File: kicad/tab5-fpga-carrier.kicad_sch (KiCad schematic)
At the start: 77 parts, among them J1 DC 12-24V, J2 USB-C PD in, J3 M5-BUS (to Tab5), J4 Tang Primer 20K Core, J5 HDMI OUT, J6 PMOD1, J7 PMOD2, J8 FPGA JTAG, Q1 2N7002, Q2 2N7002, SW1 SW, SW2 SW, U1 CH224K, U2 TPS5430DDAR, U3 AMS1117-3.3

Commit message: kicad: layout v1.0 (Core left of M5-Bus, HDMI bottom edge, pin swap), 106/106 routed, DRC clean; reset/power switch/GPIO pads; docs
Co-Authored-By: Claude Sonnet 5.5 <noreply@anthropic.com>
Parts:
- removed C7: 47u/10V, Capacitor_SMD:C_1206_3216Metric, symbol Device:C
- removed J8: FPGA JTAG, Connector_PinHeader_2.54mm:PinHeader_1x06_P2.54mm_Vertical, symbol Connector_Generic:Conn_01x06
- added C11: 22u/10V, Capacitor_SMD:C_1206_3216Metric, symbol Device:C
- added C7: 220u/10V polymer, Capacitor_SMD:CP_Elec_6.3x7.7, symbol Device:C_Polarized
- added H5, H6: M3, MountingHole:MountingHole_3.2mm_M3, symbol Mechanical:MountingHole
- added J8: GPIO pads, Connector_PinHeader_2.54mm:PinHeader_1x09_P2.54mm_Vertical, symbol Connector_Generic:Conn_01x09
- added SW3: RESET (Tab5), Button_Switch_SMD:SW_SPST_EVQP0, symbol Switch:SW_Push
- added SW4: FPGA ON/OFF, Button_Switch_THT:SW_DIP_SPSTx01_Slide_9.78x4.72mm_W7.62mm_P2.54mm, symbol Switch:SW_DIP_x01
- C10: value 22u/10V -> 10u/16V
- C9: value 10u/16V -> 47u/10V
- J6, J7: Comment 2x6 PMOD-style, 3.3V -> 2x6 PMOD-style, 3.3V. Pads only: pin header is hand-fitted 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; now not fitted
- R16: value 33R -> 0R; Comment (none) -> 16-bit extension (DNP): connects G37 to FPGA; now not fitted
- R17: value 33R -> 0R; Comment (none) -> 16-bit extension (DNP): connects G38 to FPGA; now not fitted
- R26: value 0R -> 33R; Comment 16-bit extension (DNP): connects G37 to FPGA -> (none); now fitted
- R27: value 0R -> 33R; Comment 16-bit extension (DNP): connects G38 to FPGA -> (none); now fitted
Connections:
- net +3V3: now also C11.1, J8.1 (Pin_1); no longer C10.1
- net +5V: now also C10.1, C7.1
- net BUCK_EN: now also SW4.1
- net F_AUX0: now also J4.119 (F_AUX0), R10.2; no longer J4.101 (F_AUX0), R21.2
- net F_AUX1: now also J4.109 (F_AUX1), R13.2; no longer J4.103 (F_AUX1), R22.2
- net F_AUX2: now also J4.95 (F_AUX2), R18.2; no longer J4.107 (F_AUX2), R23.2
- net F_AUX3: now also J4.91 (F_AUX3), R19.2; no longer J4.109 (F_AUX3), R24.2
- net F_BTN1: now also J4.28 (F_BTN1); no longer J4.76 (F_BTN1)
- net F_CLK: now also R23.2; no longer R14.2
- net F_D0: now also J4.113 (F_D0), R12.2; no longer J4.73 (F_D0), R10.2
- net F_D1: now also J4.107 (F_D1), R14.2; no longer J4.75 (F_D1), R11.2
- net F_D2: now also J4.103 (F_D2), R15.2; no longer J4.77 (F_D2), R12.2
- net F_D3: now also J4.85 (F_D3), R21.2; no longer J4.79 (F_D3), R13.2
- net F_D4: now also J4.89 (F_D4), R20.2; no longer J4.83 (F_D4), R15.2
- net F_D5: now also J4.79 (F_D5), R24.2; no longer J4.85 (F_D5), R16.2
- net F_D6: now also J4.83 (F_D6), R22.2; no longer J4.89 (F_D6), R17.2
- net F_D7: now also J4.75 (F_D7), R26.2; no longer J4.91 (F_D7), R18.2
- net F_DIR: now also J4.73 (F_DIR), R27.2; no longer J4.97 (F_DIR), R20.2
- net F_EXT35: now also J4.77 (F_EXT35); no longer J4.113 (F_EXT35)
- net F_EXT37: now also J4.101 (F_EXT37), R16.2; no longer J4.115 (F_EXT37), R26.2
- net F_EXT38: now also J4.97 (F_EXT38), R17.2; no longer J4.119 (F_EXT38), R27.2
- net F_HPD: now also J4.30 (F_HPD); no longer J4.78 (F_HPD)
- net F_HSCL: now also J4.36 (F_HSCL); no longer J4.152 (F_HSCL)
- net F_HSDA: now also J4.34 (F_HSDA); no longer J4.154 (F_HSDA)
- net F_LED0: now also J4.146 (F_LED0); no longer J4.50 (F_LED0)
- net F_LED1: now also J4.148 (F_LED1); no longer J4.52 (F_LED1)
- net F_LED2: now also J4.152 (F_LED2); no longer J4.56 (F_LED2)
- net F_LED3: now also J4.154 (F_LED3); no longer J4.58 (F_LED3)
- net F_RDY: now also J4.115 (F_RDY), R11.2; no longer J4.95 (F_RDY), R19.2
- net GND: now also C11.2, C7.2, J8.2 (Pin_2), SW3.2, SW4.2
- net HDMI_CKN: now also J4.142 (HDMI_CKN); no longer J4.62 (HDMI_CKN)
- net HDMI_CKP: now also J4.140 (HDMI_CKP); no longer J4.64 (HDMI_CKP)
- net HDMI_D0N: now also J4.62 (HDMI_D0N); no longer J4.142 (HDMI_D0N)
- net HDMI_D0P: now also J4.64 (HDMI_D0P); no longer J4.140 (HDMI_D0P)
- net HDMI_D1N: now also J4.70 (HDMI_D1N); no longer J4.132 (HDMI_D1N)
- net HDMI_D1P: now also J4.68 (HDMI_D1P); no longer J4.130 (HDMI_D1P)
- net HDMI_D2N: now also J4.132 (HDMI_D2N); no longer J4.70 (HDMI_D2N)
- net HDMI_D2P: now also J4.130 (HDMI_D2P); no longer J4.68 (HDMI_D2P)
- net M_AUX0: now also R10.1; no longer R21.1
- net M_AUX1: now also R13.1; no longer R22.1
- net M_AUX2: now also R18.1; no longer R23.1
- net M_AUX3: now also R19.1; no longer R24.1
- net M_CLK: now also R23.1; no longer R14.1
- net M_D0: now also R12.1; no longer R10.1
- net M_D1: now also R14.1; no longer R11.1
- net M_D2: now also R15.1; no longer R12.1
- net M_D3: now also R21.1; no longer R13.1
- net M_D4: now also R20.1; no longer R15.1
- net M_D5: now also R24.1; no longer R16.1
- net M_D6: now also R22.1; no longer R17.1
- net M_D7: now also R26.1; no longer R18.1
- net M_DIR: now also R27.1; no longer R20.1
- net M_EXT37: now also R16.1; no longer R26.1
- net M_EXT38: now also R17.1; no longer R27.1
- net M_RDY: now also R11.1; no longer R19.1
- net P1_0: now also J4.123 (P1_0); no longer J4.121 (P1_0)
- net P1_1: now also J4.92 (P1_1); no longer J4.123 (P1_1)
- net P1_2: now also J4.86 (P1_2); no longer J4.125 (P1_2)
- net P1_3: now also J4.78 (P1_3); no longer J4.129 (P1_3)
- net P1_4: now also J4.121 (P1_4); no longer J4.131 (P1_4)
- net P1_5: now also J4.90 (P1_5); no longer J4.84 (P1_5)
- net P1_6: now also J4.84 (P1_6); no longer J4.44 (P1_6)
- net P1_7: now also J4.76 (P1_7); no longer J4.46 (P1_7)
- net P2_0: now also J4.58 (P2_0); no longer J4.28 (P2_0)
- net P2_1: now also J4.52 (P2_1); no longer J4.30 (P2_1)
- net P2_2: now also J4.46 (P2_2); no longer J4.34 (P2_2)
- net P2_3: now also J4.42 (P2_3); no longer J4.36 (P2_3)
- net P2_4: now also J4.56 (P2_4); no longer J4.40 (P2_4)
- net P2_5: now also J4.50 (P2_5); no longer J4.42 (P2_5)
- net P2_6: now also J4.44 (P2_6); no longer J4.148 (P2_6)
- net P2_7: now also J4.40 (P2_7); no longer J4.146 (P2_7)
- net TAB_RST: now also SW3.1
- net GPIO3: now reaches J4.176 (GPIO3)
- net GPIO3: now also J8.6 (Pin_6)
- net GPIO2: now reaches J4.180 (GPIO2)
- net GPIO2: now also J8.5 (Pin_5)
- net GPIO1: now reaches J4.182 (GPIO1)
- net GPIO1: now also J8.4 (Pin_4)
- net GPIO0: now reaches J4.186 (GPIO0)
- net GPIO0: now also J8.3 (Pin_3)
- net JT_TCK: no longer names the net of J4.149
- net JT_TDI: no longer names the net of J4.153
- net JT_TDO: no longer names the net of J4.147
- net JT_TMS: no longer names the net of J4.143
- new net GPIO4: J4.131 (GPIO4), J8.7 (Pin_7)
- new net GPIO5: J4.129 (GPIO5), J8.8 (Pin_8)
- new net GPIO6: J4.125 (GPIO6), J8.9 (Pin_9)
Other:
- note added: "Spare FPGA I/O pads"

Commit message: kicad v2.0: Core right of M-Bus, HDMI right edge, official-Dock HDMI circuit (AC coupling/499R/ESD), coupled TMDS pair routing, 121/121 routed, DRC clean; HDMI SI study + docs/site
Co-Authored-By: Claude Sonnet 5.5 <noreply@anthropic.com>
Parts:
- removed SW3: RESET (Tab5), Button_Switch_SMD:SW_SPST_EVQP0, symbol Switch:SW_Push
- removed SW4: FPGA ON/OFF, Button_Switch_THT:SW_DIP_SPSTx01_Slide_9.78x4.72mm_W7.62mm_P2.54mm, symbol Switch:SW_DIP_x01
- added C12, C13, C14, C15, C16, C17, C18, C19: 100n, Capacitor_SMD:C_0603_1608Metric, symbol Device:C
- added R38, R39: 2.2k, Resistor_SMD:R_0603_1608Metric, symbol Device:R
- added R40: 10k, Resistor_SMD:R_0603_1608Metric, symbol Device:R
- added R41: 20k, Resistor_SMD:R_0603_1608Metric, symbol Device:R
- added R42, R43, R44, R45: 1k, Resistor_SMD:R_0603_1608Metric, symbol Device:R
- added SW3: FPGA ON/OFF, Button_Switch_THT:SW_DIP_SPSTx01_Slide_9.78x4.72mm_W7.62mm_P2.54mm, symbol Switch:SW_DIP_x01
- added U4, U5: RCLAMP0524P, Package_SON:USON-10_2.5x1.0mm_P0.5mm, symbol carrier:RCLAMP0524P
- added U6: SRV05-4, Package_TO_SOT_SMD:SOT-23-6, symbol Power_Protection:SRV05-4
- J5: Comment TMDS driven directly by FPGA true-LVDS outputs (3.3V bank) -> TMDS from FPGA true-LVDS outputs (3.3V bank), AC coupled + 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
- R16: value 0R -> 33R; Comment 16-bit extension (DNP): connects G37 to FPGA -> (none); now fitted
- R17: Comment 16-bit extension (DNP): connects G38 to FPGA -> 16-bit extension (DNP): connects G37 to FPGA
- R18: value 33R -> 0R; Comment (none) -> 16-bit extension (DNP): connects G38 to FPGA; now not fitted
- R28, R29, R32: value 10k -> 499R
- R30, R31: value 2.2k -> 499R
- R33: value 20k -> 499R
- R34, R35: value 1k -> 499R
- R36, R37: value 1k -> 10k
- SW2: value SW -> RESET (Tab5); Comment (none) -> pulls the M5-Bus RST/EN line (pin 6) low: resets the ESP32-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
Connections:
- net +3V3: now also R36.1, R37.1; no longer R28.1, R29.1
- net BUCK_EN: now also SW3.1
- net F_AUX0: now also J4.73 (F_AUX0); no longer J4.119 (F_AUX0)
- net F_AUX1: now also J4.79 (F_AUX1); no longer J4.109 (F_AUX1)
- net F_AUX2: now also R19.2; no longer R18.2
- net F_AUX3: now also J4.97 (F_AUX3), R20.2; no longer J4.91 (F_AUX3), R19.2
- net F_CLK: now also R14.2; no longer R23.2
- net F_D0: now also J4.77 (F_D0); no longer J4.113 (F_D0)
- net F_D1: now also J4.83 (F_D1), R15.2; no longer J4.107 (F_D1), R14.2
- net F_D2: now also J4.85 (F_D2), R16.2; no longer J4.103 (F_D2), R15.2
- net F_D3: now also J4.103 (F_D3), R22.2; no longer J4.85 (F_D3), R21.2
- net F_D4: now also J4.101 (F_D4), R21.2; no longer J4.89 (F_D4), R20.2
- net F_D5: now also J4.109 (F_D5); no longer J4.79 (F_D5)
- net F_D6: now also J4.107 (F_D6), R23.2; no longer J4.83 (F_D6), R22.2
- net F_D7: now also J4.115 (F_D7); no longer J4.75 (F_D7)
- net F_DIR: now also J4.119 (F_DIR); no longer J4.73 (F_DIR)
- net F_EXT35: now also J4.113 (F_EXT35); no longer J4.77 (F_EXT35)
- net F_EXT37: now also J4.89 (F_EXT37), R17.2; no longer J4.101 (F_EXT37), R16.2
- net F_EXT38: now also J4.91 (F_EXT38), R18.2; no longer J4.97 (F_EXT38), R17.2
- net F_HPD: now also R40.2, R41.1; no longer R32.2, R33.1
- net F_HSCL: now also R36.2; no longer R28.2
- net F_HSDA: now also R37.2; no longer R29.2
- net F_LED0: now also R42.1; no longer R34.1
- net F_LED1: now also R43.1; no longer R35.1
- net F_LED2: now also R44.1; no longer R36.1
- net F_LED3: now also R45.1; no longer R37.1
- net F_RDY: now also J4.75 (F_RDY); no longer J4.115 (F_RDY)
- net GND: now also R28.2, R29.2, R30.2, R31.2, R32.2, R34.2, R35.2, R41.2, SW3.2, U4.3 (GND), U4.8 (GND), U5.3 (GND), U5.8 (GND), U6.2 (VN)
- net GPIO0: now also J4.125 (GPIO0); no longer J4.186 (GPIO0)
- net GPIO1: now also J4.129 (GPIO1); no longer J4.182 (GPIO1)
- net GPIO2: now also J4.131 (GPIO2); no longer J4.180 (GPIO2)
- net GPIO4: now also J4.180 (GPIO4); no longer J4.131 (GPIO4)
- net GPIO5: now also J4.182 (GPIO5); no longer J4.129 (GPIO5)
- net GPIO6: now also J4.186 (GPIO6); no longer J4.125 (GPIO6)
- net HDMI_5V: now also R38.1, R39.1, U6.5 (VP); no longer R30.1, R31.1
- net HDMI_CKN: now also C19.1; no longer J5.12 (CK-)
- net HDMI_CKP: now also C18.1; no longer J5.10 (CK+)
- net HDMI_D0N: now also J4.132 (HDMI_D0N), C17.1; no longer J4.62 (HDMI_D0N), J5.9 (D0-)
- net HDMI_D0P: now also J4.130 (HDMI_D0P), C16.1; no longer J4.64 (HDMI_D0P), J5.7 (D0+)
- net HDMI_D1N: now also C15.1; no longer J5.6 (D1-)
- net HDMI_D1P: now also C14.1; no longer J5.4 (D1+)
- net HDMI_D2N: now also J4.58 (HDMI_D2N), C13.1; no longer J4.132 (HDMI_D2N), J5.3 (D2-)
- net HDMI_D2P: now also J4.56 (HDMI_D2P), C12.1; no longer J4.130 (HDMI_D2P), J5.1 (D2+)
- net HDMI_HPD: now also R40.1, U6.3 (IO2); no longer R32.1
- net HDMI_SCL: now also R38.2, U6.4 (IO3); no longer R30.2
- net HDMI_SDA: now also R39.2, U6.6 (IO4); no longer R31.2
- net LED0_A: now also R42.2; no longer R34.2
- net LED1_A: now also R43.2; no longer R35.2
- net LED2_A: now also R44.2; no longer R36.2
- net LED3_A: now also R45.2; no longer R37.2
- net M_AUX2: now also R19.1; no longer R18.1
- net M_AUX3: now also R20.1; no longer R19.1
- net M_CLK: now also R14.1; no longer R23.1
- net M_D1: now also R15.1; no longer R14.1
- net M_D2: now also R16.1; no longer R15.1
- net M_D3: now also R22.1; no longer R21.1
- net M_D4: now also R21.1; no longer R20.1
- net M_D6: now also R23.1; no longer R22.1
- net M_EXT37: now also R17.1; no longer R16.1
- net M_EXT38: now also R18.1; no longer R17.1
- net P1_0: now also J4.76 (P1_0); no longer J4.123 (P1_0)
- net P1_1: now also J4.84 (P1_1); no longer J4.92 (P1_1)
- net P1_2: now also J4.90 (P1_2); no longer J4.86 (P1_2)
- net P1_3: now also J4.121 (P1_3); no longer J4.78 (P1_3)
- net P1_4: now also J4.78 (P1_4); no longer J4.121 (P1_4)
- net P1_5: now also J4.86 (P1_5); no longer J4.90 (P1_5)
- net P1_6: now also J4.92 (P1_6); no longer J4.84 (P1_6)
- net P1_7: now also J4.123 (P1_7); no longer J4.76 (P1_7)
- net P2_0: now also J4.40 (P2_0); no longer J4.58 (P2_0)
- net P2_1: now also J4.44 (P2_1); no longer J4.52 (P2_1)
- net P2_2: now also J4.50 (P2_2); no longer J4.46 (P2_2)
- net P2_3: now also J4.62 (P2_3); no longer J4.42 (P2_3)
- net P2_4: now also J4.42 (P2_4); no longer J4.56 (P2_4)
- net P2_5: now also J4.46 (P2_5); no longer J4.50 (P2_5)
- net P2_6: now also J4.52 (P2_6); no longer J4.44 (P2_6)
- net P2_7: now also J4.64 (P2_7); no longer J4.40 (P2_7)
- net TAB_RST: now also SW2.1
- net F_BTN1: no longer names the net of J4.28
- net F_BTN1: no longer SW2.1
- new net HDMI_CKN_C: C19.2, R35.1, U5.5 (IN4)
- new net HDMI_CKN_K: J5.12 (CK-), U5.6 (OUT4)
- new net HDMI_CKP_C: C18.2, R34.1, U5.4 (IN3)
- new net HDMI_CKP_K: J5.10 (CK+), U5.7 (OUT3)
- new net HDMI_D0N_C: C17.2, R33.1, U5.2 (IN2)
- new net HDMI_D0N_K: J5.9 (D0-), U5.9 (OUT2)
- new net HDMI_D0P_C: C16.2, R32.1, U5.1 (IN1)
- new net HDMI_D0P_K: J5.7 (D0+), U5.10 (OUT1)
- new net HDMI_D1N_C: C15.2, R31.1, U4.5 (IN4)
- new net HDMI_D1N_K: J5.6 (D1-), U4.6 (OUT4)
- new net HDMI_D1P_C: C14.2, R30.1, U4.4 (IN3)
- new net HDMI_D1P_K: J5.4 (D1+), U4.7 (OUT3)
- new net HDMI_D2N_C: C13.2, R29.1, U4.2 (IN2)
- new net HDMI_D2N_K: J5.3 (D2-), U4.9 (OUT2)
- new net HDMI_D2P_C: C12.2, R28.1, U4.1 (IN1)
- new net HDMI_D2P_K: J5.1 (D2+), U4.10 (OUT1)
- no-connect marks 8 -> 9
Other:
- note added: "HDMI OUT connector + DDC/HPD level shift + ESD"
- note added: "HDMI TMDS 499R bias, ESD"
- note added: "HDMI TMDS AC coupling caps"
- note removed: "HDMI OUT (TMDS direct from FPGA) + DDC/HPD level shift"

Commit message: HDMI remediation after independent audit: copper-continuous ESD, short 499R branches, re-routed pairs, re-simulated channel
- ESD (RClamp0524P, C293965): I/O pins joined to the TMDS line by copper straps, no reliance on part-internal pass-through
- 499 ohm bias resistors moved next to the tap (branches 2-11.5 mm), routed and modelled as terminated lines
- route_pcb: roles JSON (main/branch), pair routing, 113/113 nets, DRC 0/0
- sim: ordered-segment extraction without silent fallback, branch/ESD channel model, continuity check, variants
- report page, docs (section 10), README, BOM updated; open items disclosed (D1N branch 11.5 mm, 3D uncalibrated)

Co-Authored-By: Claude Sonnet 5.5 <noreply@anthropic.com>
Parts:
- U4, U5: Comment TMDS ESD array as on the official Dock (flow-through) -> TMDS ESD array (DOWO DFN2510-10L): I/O 1,2,4,5, GND 3,8; th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
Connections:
- net HDMI_CKN_K is gone; now on net HDMI_CKN_C: J5.12 (CK-), U5.6 (OUT4)
- net HDMI_CKP_K is gone; now on net HDMI_CKP_C: J5.10 (CK+), U5.7 (OUT3)
- net HDMI_D0N_K is gone; now on net HDMI_D0N_C: J5.9 (D0-), U5.9 (OUT2)
- net HDMI_D0P_K is gone; now on net HDMI_D0P_C: J5.7 (D0+), U5.10 (OUT1)
- net HDMI_D1N_K is gone; now on net HDMI_D1N_C: J5.6 (D1-), U4.6 (OUT4)
- net HDMI_D1P_K is gone; now on net HDMI_D1P_C: J5.4 (D1+), U4.7 (OUT3)
- net HDMI_D2N_K is gone; now on net HDMI_D2N_C: J5.3 (D2-), U4.9 (OUT2)
- net HDMI_D2P_K is gone; now on net HDMI_D2P_C: J5.1 (D2+), U4.10 (OUT1)

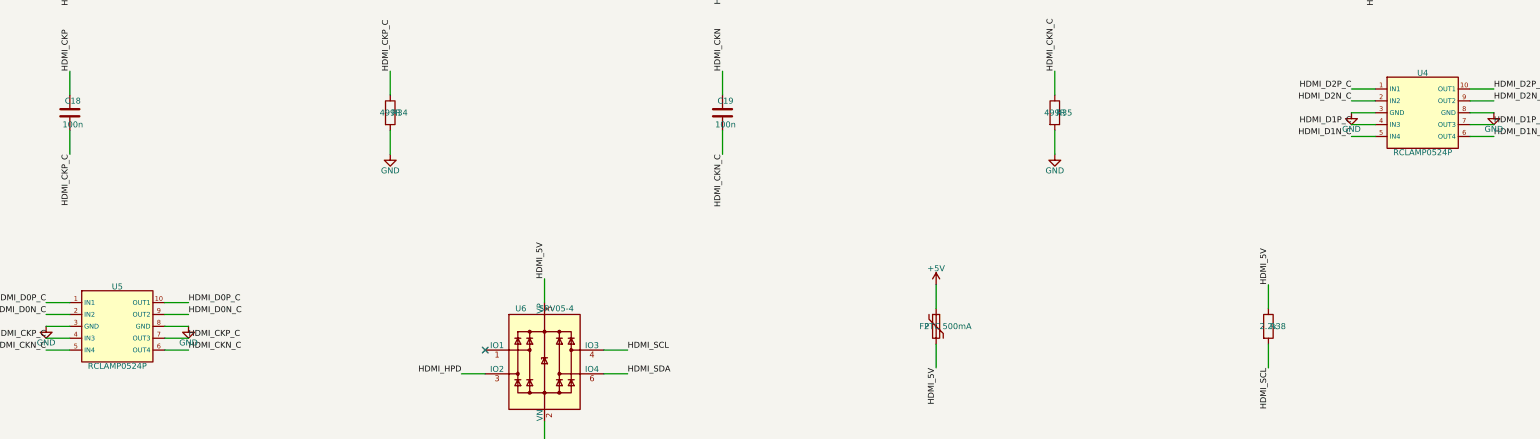
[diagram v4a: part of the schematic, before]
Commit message: HDMI second-audit remediation (A1-A5): ESD footprint, escape stubs, 4-port P/N model, combined sensitivity, checks, report r3
- A1: dedicated DFN2510-10L_RCLAMP0524P footprint (GND land 0.30->0.42 mm), symbol IO/NC, datasheet comparison + check_esd_footprint.py
- A2: router roles stub/strap, check_classification.py (0 unclassified), pad-clipped escape stubs added to the analysed path
- A3: 4-port P/N ABCD channel model, P/N branches at their own taps, SCD21; short-symmetric-branch comparison
- A4: Core Z x ESD C matrix; fails -10 dB at Core 85 ohm with ESD >= 0.35 pF (D1)
- A5: check_continuity pin-number check + exit codes, check_negative.py, manifest_r3.json, D2 inversion doc, README/site updated
- New report site/hdmi-simulation-r3.html (r1/r2 kept); re-routed 113/113 nets, DRC 0/0
- Not done: 3D calibration (B), MeOS requirements (C)

Co-Authored-By: Claude Sonnet 5.5 <noreply@anthropic.com>
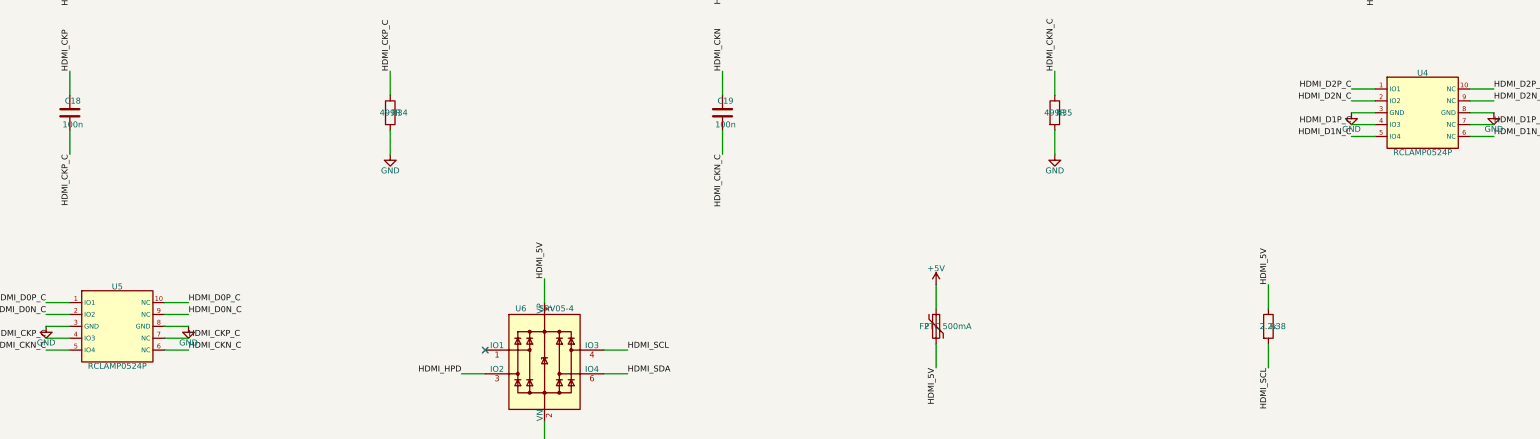
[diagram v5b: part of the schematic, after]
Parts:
- U4, U5: footprint Package_SON:USON-10_2.5x1.0mm_P0.5mm -> carrier:DFN2510-10L_RCLAMP0524P
